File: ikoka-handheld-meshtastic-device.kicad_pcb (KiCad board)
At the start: 2 copper layers, 40 x 55 mm, 41 parts, among them J1 Conn_Coaxial, J4 1.25-2PWB, Q1 AO3401A, SW1 SW_Push, SW2 SW_Push, U1 MT3608B, U2 E22-900M30S, U3 XIAO-nRF52840-SMD, U4 TP4056-42-ESOP8

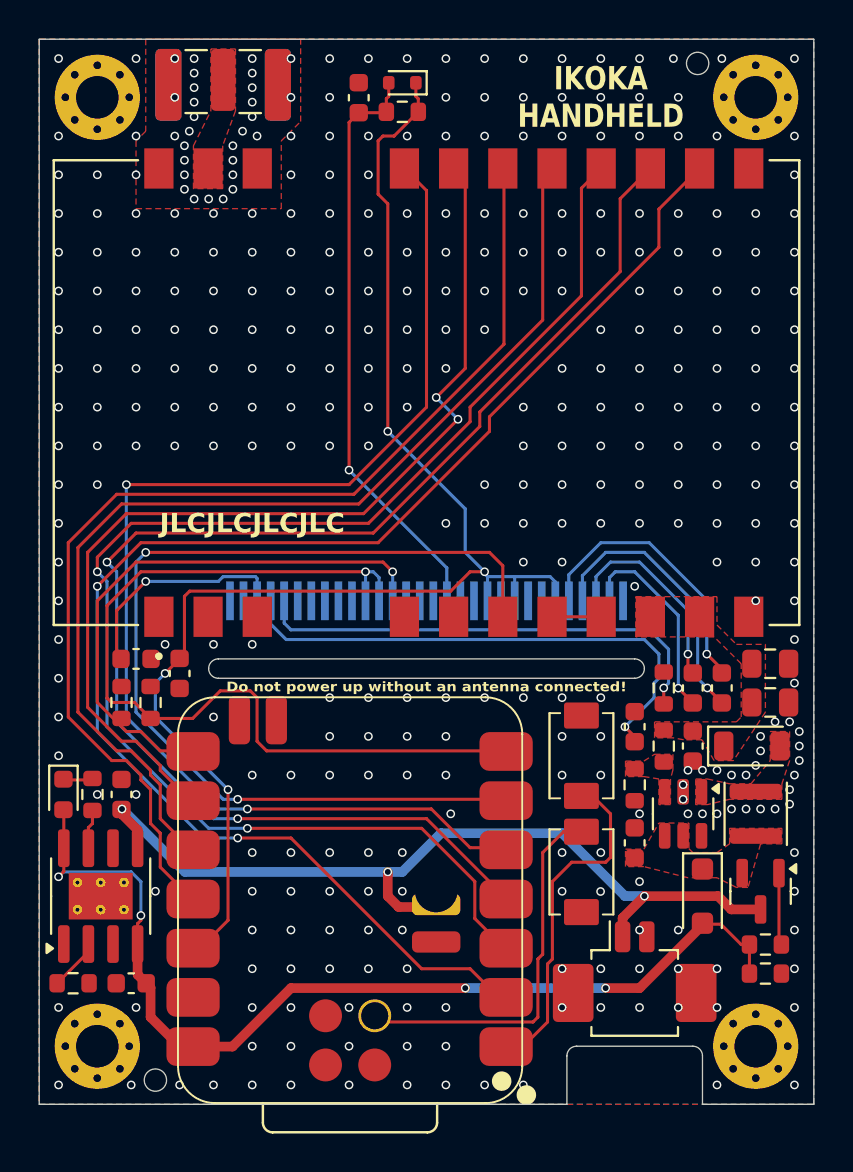
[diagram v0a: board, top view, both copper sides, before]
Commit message: fix: OLED did not need to be mirrored, add pin 1 & 30 silk
Signed-off-by: Andrew Yong <me@ndoo.sg>
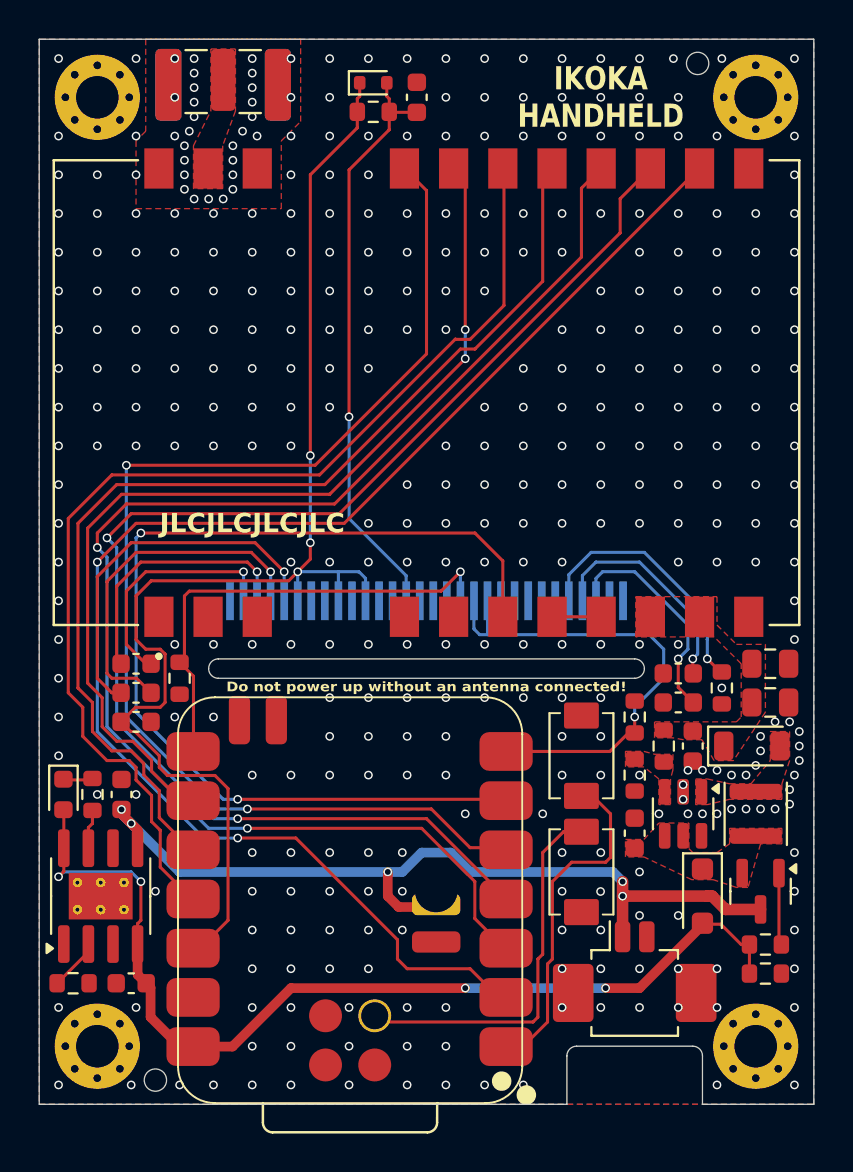
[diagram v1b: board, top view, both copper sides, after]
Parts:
- DS1: footprint Display:OLED-128O064D_ReverseMount -> Display:OLED-128O064D
- moved C8 30.3 mm to (135.0, 78.8), turned to 0 degrees
- moved C9 28.8 mm to (135.0, 77.2), turned to 0 degrees
- moved C6 28.1 mm to (163.0, 79.2), turned to 180 degrees
- moved R6 25.0 mm to (160.8, 80.0)
- moved C7 3.55 mm to (163.0, 77.8), turned to 180 degrees
- moved C5 3.36 mm to (135.0, 80.2), turned to 0 degrees
- moved R7 3.25 mm to (137.2, 78.0), turned to -90 degrees
- moved C10 3.00 mm to (149.5, 48.0)
- moved R5 3.00 mm to (165.2, 78.5), turned to -90 degrees
- moved D2 1.50 mm to (147.2, 47.2), turned to 0 degrees
- moved R8 1.50 mm to (147.2, 48.8), turned to 0 degrees
- moved C1 0.50 mm to (160.8, 86.0)
- moved R2 0.50 mm to (160.8, 83.0)
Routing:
- net /I2C_SDA: track 46.6 -> 25.4 mm
- net Net-(DS1-VCOMH): track 27.4 -> 11.6 mm
- net Net-(DS1-IREF): track 24.5 -> 13.6 mm
- net Net-(DS1-C1N): track 14.5 -> 19.3 mm
- net +3V3: track 73.5 -> 69.0 mm, vias 4 -> 3
- net /I2C_SCL: track 29.0 -> 24.7 mm
- net Net-(DS1-C1P): track 14.4 -> 18.4 mm
- net Net-(DS1-C2P): track 10.7 -> 13.6 mm
- net Net-(DS1-C2N): track 10.6 -> 12.4 mm
- net /LORA_RXEN: track 50.9 -> 52.6 mm
- net /LORA_SPI_NSS: track 64.4 -> 63.4 mm
- net /LORA_BUSY: track 71.5 -> 70.6 mm
- net /LORA_RST: track 73.5 -> 72.6 mm
- net /LORA_SPI_SCK: track 51.8 -> 51.2 mm
- net +BATT: vias 3 -> 5
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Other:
- board text added: "1"
- board text added: "30"

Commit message: feat: Use more 1.5k and 300k resistors where possible to simplify BoM
Signed-off-by: Andrew Yong <me@ndoo.sg>
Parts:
- R10, R4: value 1k -> 1.5k
- R3: value 100k -> 300k
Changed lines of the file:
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@@
 			)
 		)
-		(property "Value" "1k"
+		(property "Value" "1.5k"
 			(at 0 1.43 90)
 			(layer "F.Fab")
@@
 			)
 		)
-		(property "Value" "100k"
+		(property "Value" "300k"
 			(at 0 1.43 0)
 			(layer "F.Fab")
@@
 			)
 		)
-		(property "Value" "1k"
+		(property "Value" "1.5k"
 			(at 0 1.43 0)
 			(layer "F.Fab")

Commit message: feat(pcbnew): Improve layout
- All SX1262 traces to the back
- Don't run SSD1306 charge pump and SX1262 traces on top of each other in parallel
- Move SSD1306 reset circuit to bottom half of PCB

Signed-off-by: Andrew Yong <me@ndoo.sg>
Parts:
- moved C10 37.4 mm to (131.5, 80.8), turned to -90 degrees
- moved D2 35.8 mm to (134.5, 80.8), turned to 90 degrees
- moved R8 35.0 mm to (133.0, 80.8), turned to 90 degrees
- moved C8 3.64 mm to (131.5, 77.8), turned to 90 degrees
- moved C5 2.47 mm to (136.8, 78.5)
- moved C9 2.06 mm to (133.0, 77.8), turned to -90 degrees
- moved R7 1.12 mm to (136.8, 77.0), turned to 0 degrees
- moved C12 0.35 mm to (134.5, 83.8)
- moved D4 0.35 mm to (131.5, 83.8)
- moved R10 0.35 mm to (133.0, 83.8)
- moved C11 0.25 mm to (134.8, 93.5)
- moved R9 0.25 mm to (131.8, 93.5)
- moved U4 0.25 mm to (133.2, 89.0)
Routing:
- net +3V3: track 69.0 -> 40.0 mm, vias 3 -> 1
- net /LORA_RST: track 72.6 -> 66.2 mm
- net /LORA_SPI_NSS: track 63.4 -> 57.6 mm
- net /LORA_DIO1: track 75.7 -> 70.7 mm
- net /LORA_BUSY: track 70.6 -> 66.0 mm
- net /I2C_SCL: track 24.7 -> 28.0 mm
- net Net-(DS1-C1N): track 19.3 -> 22.0 mm
- net Net-(D2-A): track 30.3 -> 32.9 mm, vias 1 -> 3
- net Net-(DS1-C2N): track 12.4 -> 14.9 mm
- net /LORA_RXEN: track 52.6 -> 54.1 mm
- net Net-(DS1-C2P): track 13.6 -> 14.8 mm
- net /LORA_SPI_MOSI: track 57.2 -> 55.9 mm, vias 0 -> 2
- net /LORA_SPI_MISO: track 55.2 -> 56.1 mm, vias 0 -> 2
- net /LORA_SPI_SCK: track 51.2 -> 52.1 mm
- net GND: vias 383 -> 380

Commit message: feat: OSHW logo
Signed-off-by: Andrew Yong <me@ndoo.sg>
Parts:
- added SYM1: Logo_Open_Hardware_Small, Symbol:OSHW-Logo_19x20mm_SilkScreen, B.Cu at (150.2, 60.0)
